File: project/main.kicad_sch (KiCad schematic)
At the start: 191 parts

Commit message: adding storage project
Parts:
- renumbered R84 to R61, R61 to R62, R62 to R63, R63 to R64, R64 to R65, R65 to R66, R66 to R67, R67 to R68, R68 to R69, R69 to R70, R70 to R71, R71 to R72, R72 to R73, R73 to R74, R74 to R75, R75 to R76, R76 to R77, R77 to R78, R78 to R79, R79 to R80, R80 to R81, R81 to R82, R82 to R83, R83 to R84

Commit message: configuring kibot for both projects
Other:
- title: space -> main
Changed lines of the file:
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@@
   (paper "A4")
   (title_block
-    (title "space")
-    (date "2024-02-05")
+    (title "main")
+    (date "2024-02-16")
     (rev "5.0")
     (company "makerspace.lt")

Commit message: updating main base dimensions
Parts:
- added R36: sheet boards, -local:_o_sheet_boards__, symbol Device:R
- added R37: sheet metal, -local:_o_sheet_matal__, symbol Device:R
- R41: renamed from R39; value palet rack -> palet rack metal
- R42: renamed from R40; value palet rack -> palet rack wood
- renumbered R98 to R100, R99 to R101, R100 to R102, R101 to R103, R102 to R104, R36 to R38, R37 to R39, R38 to R40, R41 to R43, R42 to R44, R43 to R45, R44 to R46, R45 to R47, R46 to R48, R47 to R49, R48 to R50, R49 to R51, R50 to R52, R51 to R53, R52 to R54, R53 to R55, R54 to R56, R55 to R57, R56 to R58, R57 to R59, R58 to R60, R59 to R61, R60 to R62, R61 to R63, R62 to R64, R63 to R65, R64 to R66, R65 to R67, R66 to R68, R67 to R69, R68 to R70, R69 to R71, R70 to R72, R71 to R73, R72 to R74, R73 to R75, R74 to R76, R75 to R77, R76 to R78, R77 to R79, R78 to R80, R79 to R81, R80 to R82, R81 to R83, R82 to R84, R83 to R85, R84 to R86, R85 to R87, R86 to R88, R87 to R89, R88 to R90, R89 to R91, R90 to R92, R91 to R93, R92 to R94, R93 to R95, R94 to R96, R95 to R97, R96 to R98, R97 to R99

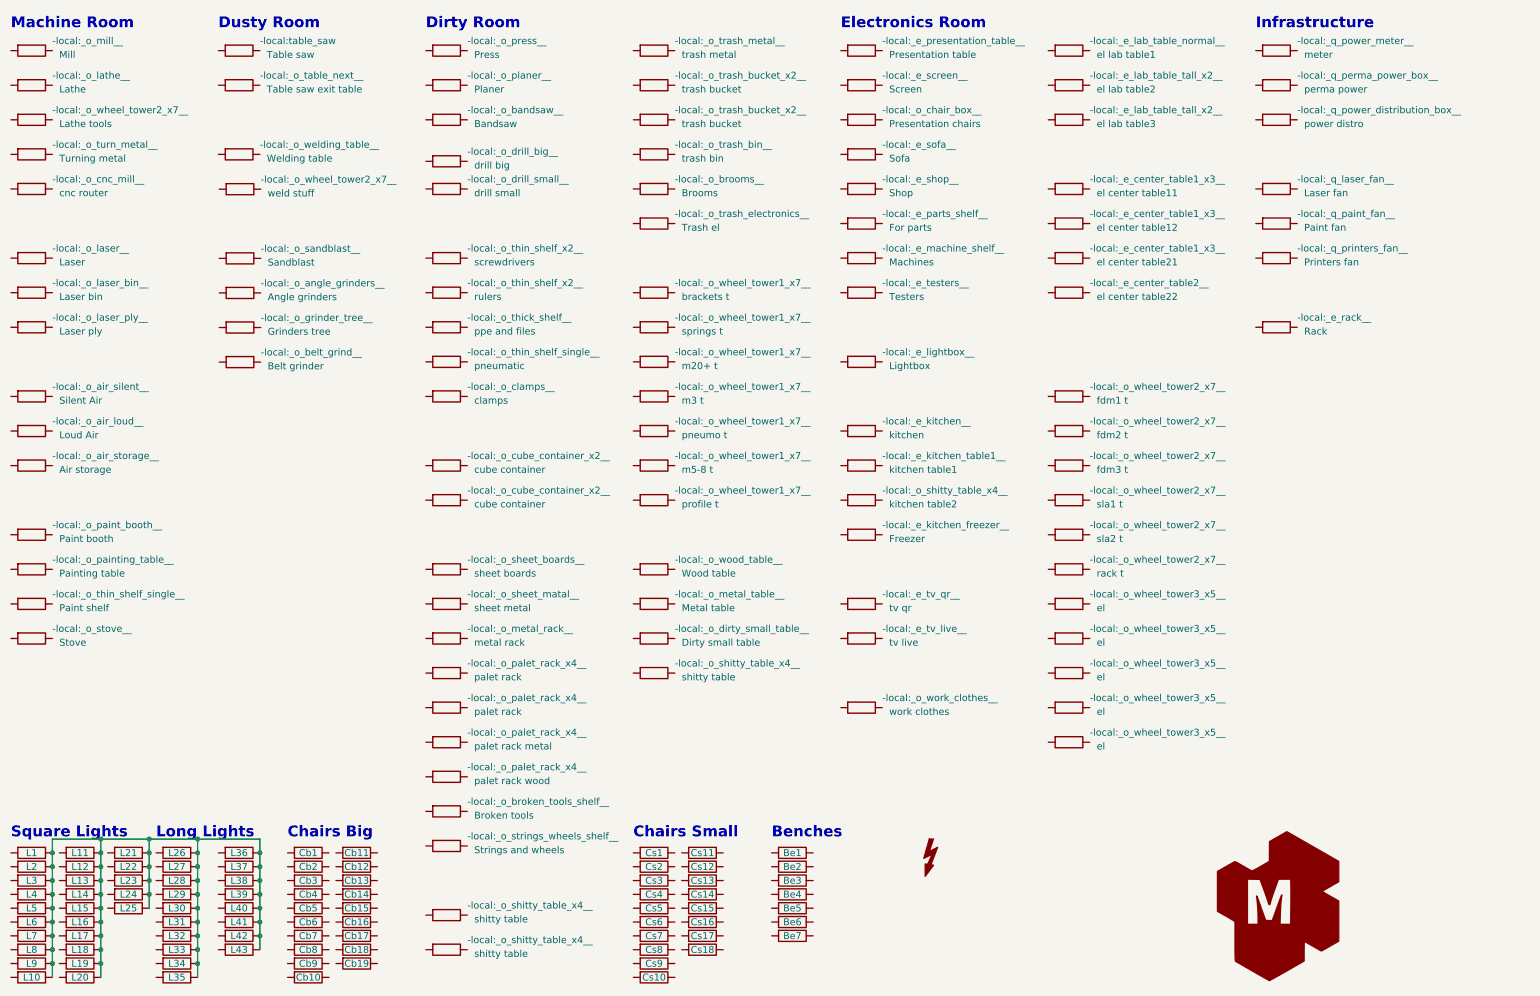
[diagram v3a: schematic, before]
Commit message: updating main base dimensions and fixing all the things
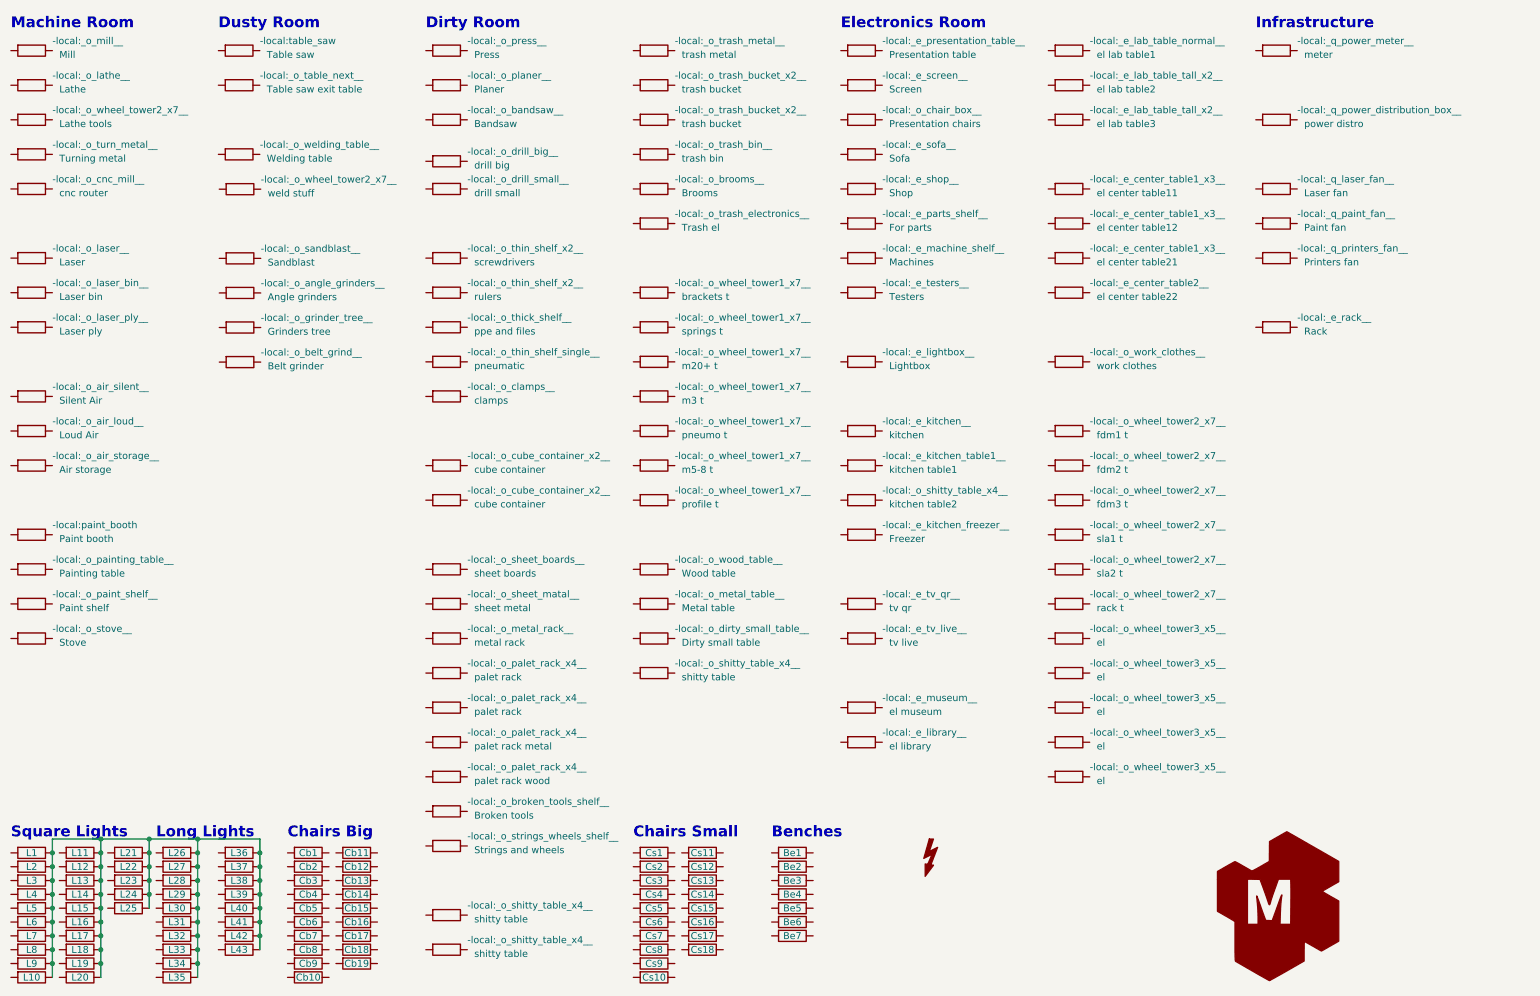
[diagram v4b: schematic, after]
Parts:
- removed R99: perma power, -local:_q_perma_power_box__, symbol Device:R
- added R79: el museum, -local:_e_museum__, symbol Device:R
- added R80: el library, -local:_e_library__, symbol Device:R
- R12: footprint -local:_o_paint_booth__ -> -local:paint_booth
- R14: footprint -local:_o_thin_shelf_single__ -> -local:_o_paint_shelf__
- renumbered R98 to R100, R100 to R101, R101 to R102, R102 to R103, R103 to R104, R104 to R105, R80 to R81, R81 to R82, R82 to R83, R83 to R84, R84 to R85, R85 to R86, R86 to R87, R79 to R88, R87 to R89, R88 to R90, R89 to R91, R90 to R92, R91 to R93, R92 to R94, R93 to R95, R94 to R96, R95 to R97, R96 to R98, R97 to R99

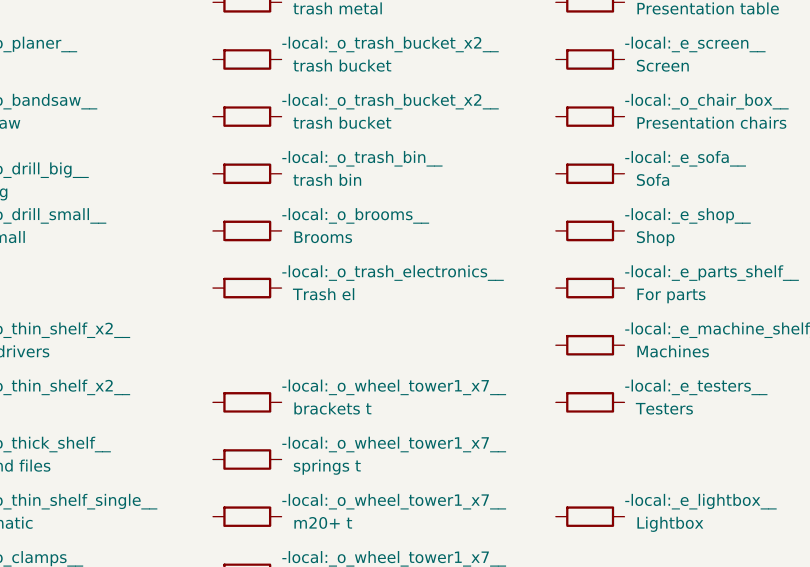
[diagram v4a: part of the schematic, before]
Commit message: alternate placement for dirty workshop
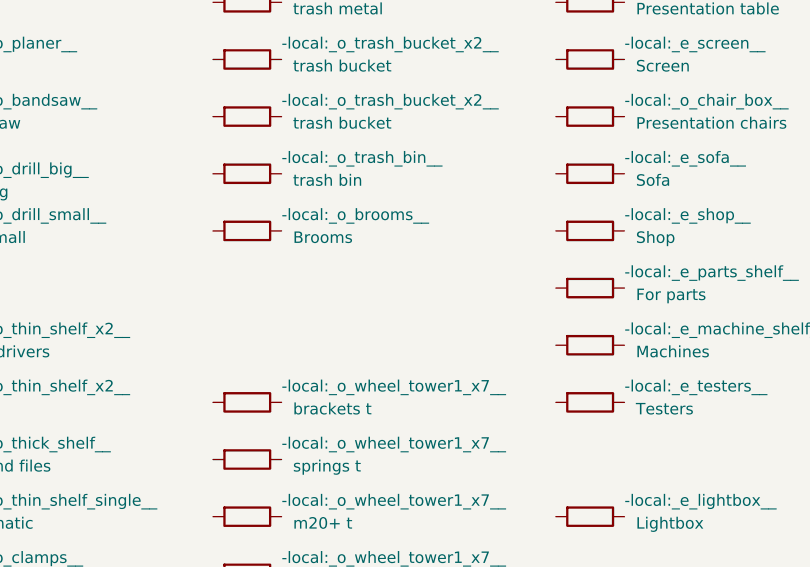
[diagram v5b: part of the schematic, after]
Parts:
- removed R52: Trash el, -local:_o_trash_electronics__, symbol Device:R
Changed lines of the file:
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@@
-    (pin "2")
-  )
-  (symbol (lib_id "Device:R") (at 130.81 57.15 270) (unit 1)
-    (in_bom yes) (on_board yes)
-    (property "Reference" "R52" (id 0) (at 130.81 48.26 90)
-      (effects (font (size 1.27 1.27)) hide)
-    )
-    (property "Value" "Trash el" (id 1) (at 135.89 57.15 90)
-      (effects (font (size 1.27 1.27)) (justify left top))
-    )
-    (property "Footprint" "-local:_o_trash_electronics__" (id 2) (at 134.62 54.61 90)
-      (effects (font (size 1.27 1.27)) (justify left top))
-    )
-    (property "Datasheet" "~" (id 3) (at 130.81 57.15 0)
-      (effects (font (size 1.27 1.27)) hide)
-    )
-    (pin "1")
     (pin "2")
   )
@@
       (reference "R51") (unit 1) (value "Brooms") (footprint "-local:_o_brooms__")
     )
-    (path "/e8945538-4119-43cb-a645-97184f94995d"
-      (reference "R52") (unit 1) (value "Trash el") (footprint "-local:_o_trash_electronics__")
-    )
     (path "/67d7ca95-c2ce-4cf8-974e-f28e2ae17ec6"

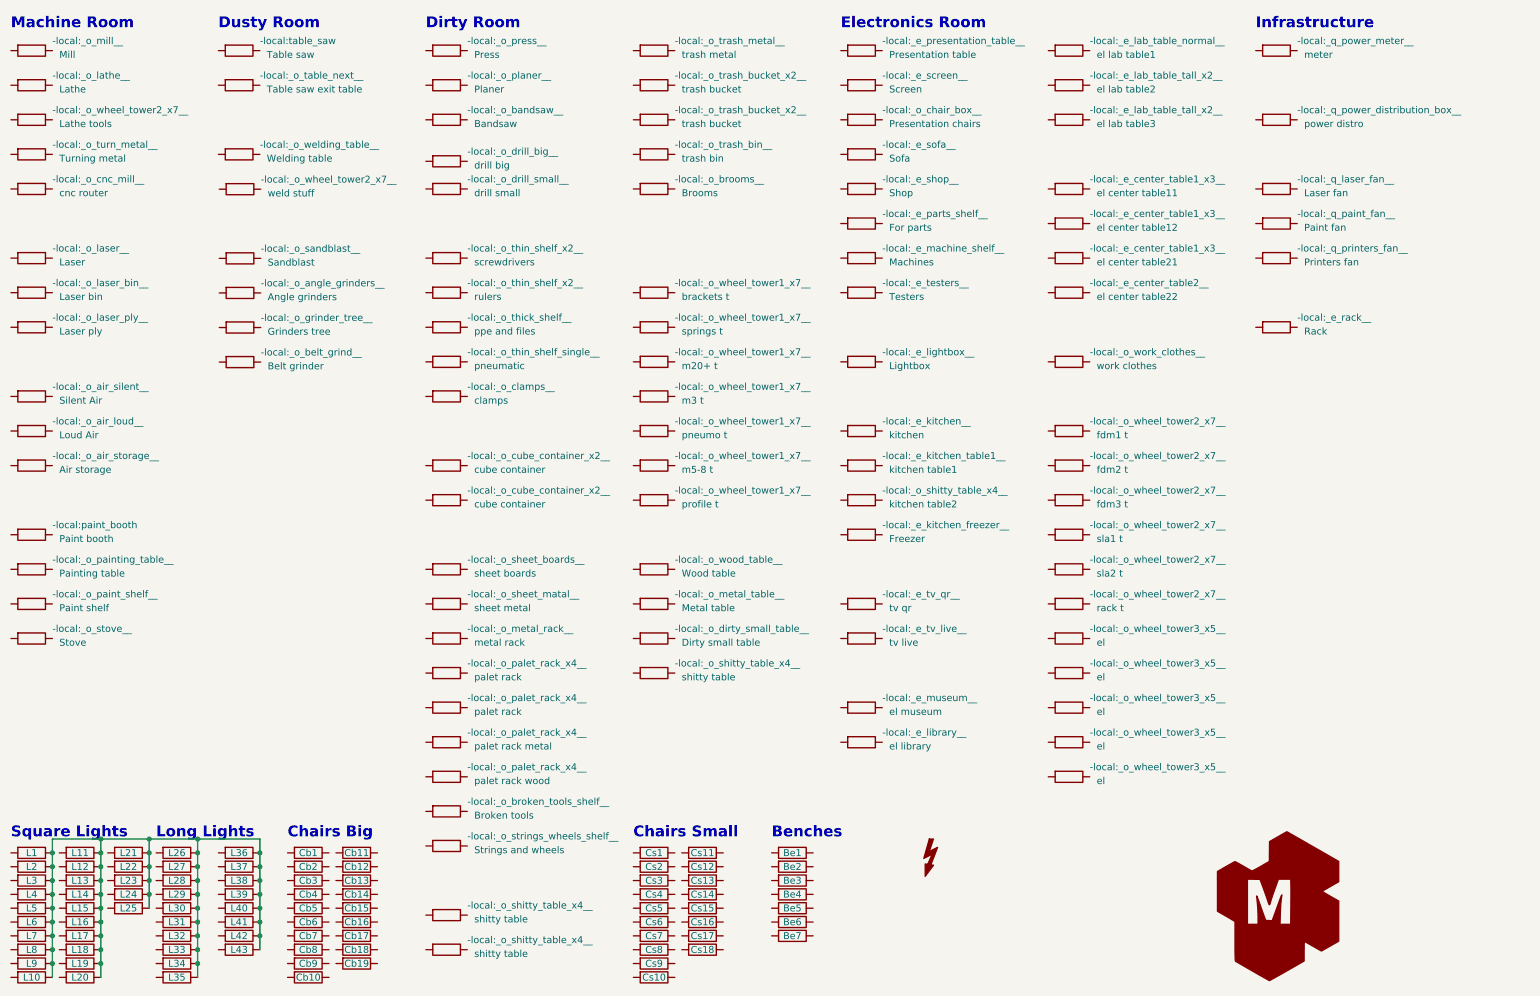
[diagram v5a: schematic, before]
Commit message: adding power cable runs
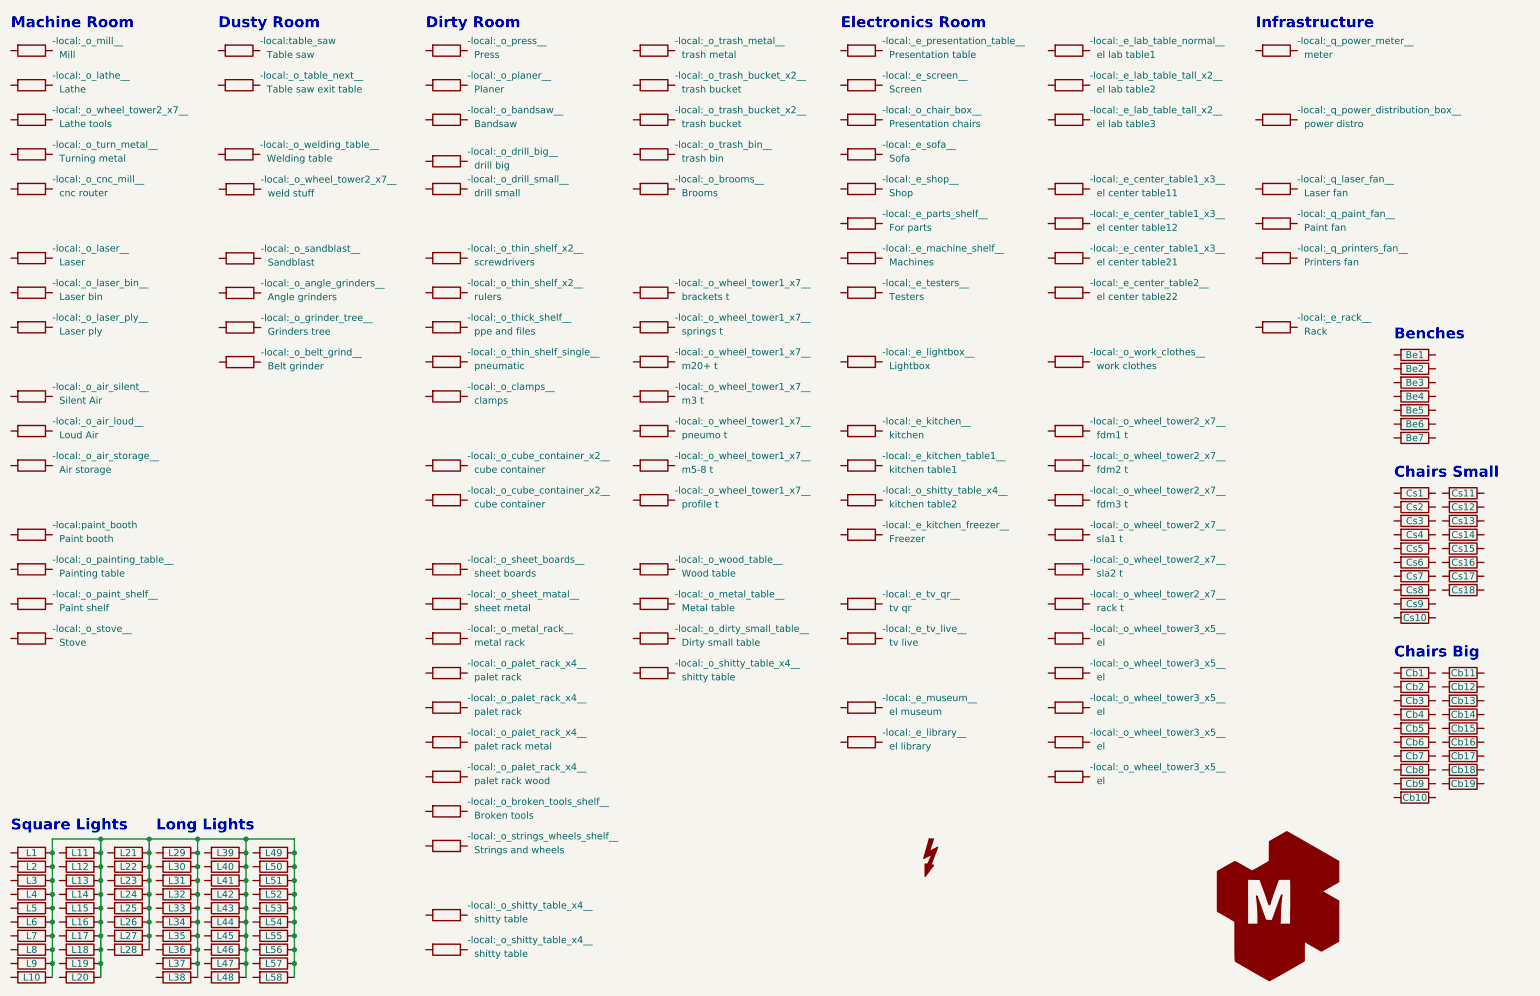
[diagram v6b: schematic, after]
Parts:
- added L26, L27, L28: light, -local:light_square, symbol Device:R
- added L47, L48, L49, L50, L51, L52, L53, L54, L55, L56, L57, L58: light, -local:light_long, symbol Device:R
- renumbered L26 to L29, L27 to L30, L28 to L31, L29 to L32, L30 to L33, L31 to L34, L32 to L35, L33 to L36, L34 to L37, L35 to L38, L36 to L39, L37 to L40, L38 to L41, L39 to L42, L40 to L43, L41 to L44, L42 to L45, L43 to L46, R101 to R100, R102 to R101, R103 to R102, R104 to R103, R105 to R104, R53 to R52, R54 to R53, R55 to R54, R56 to R55, R57 to R56, R58 to R57, R59 to R58, R60 to R59, R61 to R60, R62 to R61, R63 to R62, R64 to R63, R65 to R64, R66 to R65, R67 to R66, R68 to R67, R69 to R68, R70 to R69, R71 to R70, R72 to R71, R73 to R72, R74 to R73, R75 to R74, R76 to R75, R77 to R76, R78 to R77, R79 to R78, R80 to R79, R81 to R80, R82 to R81, R83 to R82, R84 to R83, R85 to R84, R86 to R85, R87 to R86, R88 to R87, R89 to R88, R90 to R89, R91 to R90, R92 to R91, R93 to R92, R94 to R93, R95 to R94, R96 to R95, R97 to R96, R98 to R97, R99 to R98, R100 to R99
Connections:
- net at L1.1, L10.1, L11.1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: now also L26.1, L27.1, L28.1, L47.1, L48.1, L49.1, L50.1, L51.1, L52.1, L53.1, L54.1, L55.1, L56.1, L57.1, L58.1
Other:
- moved on the sheet: Be1, Be2, Be3, Be4, Be5, Be6, Be7, Cb1, Cb10, Cb11, Cb12, Cb13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

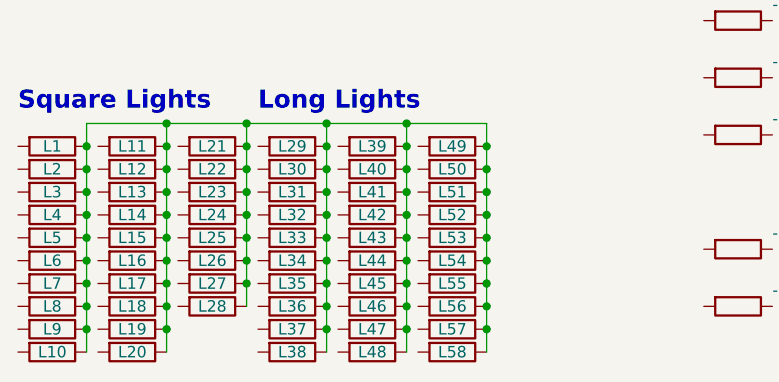
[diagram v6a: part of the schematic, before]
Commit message: small tweeks and fixes as we implement the plan
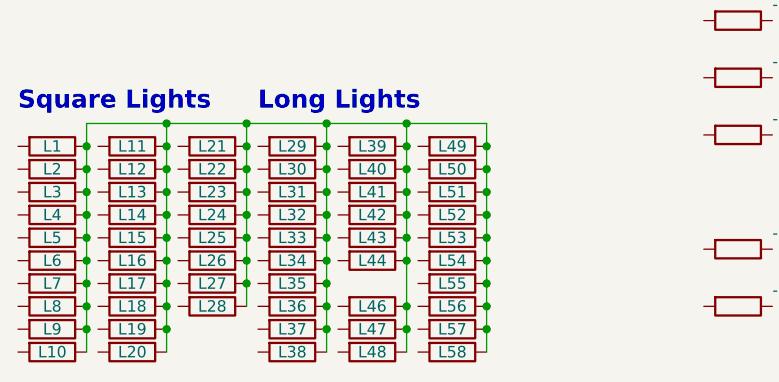
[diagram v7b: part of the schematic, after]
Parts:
- removed L45: light, -local:light_long, symbol Device:R
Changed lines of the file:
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@@
   (junction (at 55.88 182.88) (diameter 0) (color 0 0 0 0)
   )
-  (junction (at 55.88 187.96) (diameter 0) (color 0 0 0 0)
-  )
   (junction (at 20.32 177.8) (diameter 0) (color 0 0 0 0)
   )
@@
   (junction (at 38.1 172.72) (diameter 0) (color 0 0 0 0)
   )
-  (wire (pts (xy 55.88 187.96) (xy 55.88 190.5))
+  (wire (pts (xy 55.88 185.42) (xy 55.88 190.5))
     (stroke (width 0) (type default) (color 0 0 0 0))
   )
@@
     (stroke (width 0) (type default) (color 0 0 0 0))
   )
-  (wire (pts (xy 55.88 185.42) (xy 55.88 187.96))
-    (stroke (width 0) (type default) (color 0 0 0 0))
-  )
   (wire (pts (xy 55.88 170.18) (xy 64.77 170.18))
     (stroke (width 0) (type default) (color 0 0 0 0))
@@
     (pin "2")
   )
-  (symbol (lib_id "Device:R") (at 52.07 187.96 270) (unit 1)
-    (in_bom yes) (on_board yes)
-    (property "Reference" "L45" (id 0) (at 52.07 187.96 90))
-    (property "Value" "light" (id 1) (at 57.15 187.96 90)
-      (effects (font (size 1.27 1.27)) (justify left top) hide)
-    )
-    (property "Footprint" "-local:light_long" (id 2) (at 55.88 185.42 90)
-      (effects (font (size 1.27 1.27)) (justify left top) hide)
-    )
-    (property "Datasheet" "~" (id 3) (at 52.07 187.96 0)
-      (effects (font (size 1.27 1.27)) hide)
-    )
-    (pin "1")
-    (pin "2")
-  )
   (symbol (lib_id "Device:R") (at 207.01 95.25 270) (unit 1)
     (in_bom yes) (on_board yes)
@@
       (reference "L44") (unit 1) (value "light") (footprint "-local:light_long")
     )
-    (path "/8e001a81-9851-40d7-943e-c39f30ad2bc2"
-      (reference "L45") (unit 1) (value "light") (footprint "-local:light_long")
-    )
     (path "/71cba61a-ddc8-4b09-b81a-194caa739dc0"
